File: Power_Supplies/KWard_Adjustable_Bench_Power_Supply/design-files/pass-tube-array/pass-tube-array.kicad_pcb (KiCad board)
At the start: 2 copper layers, 142.9 x 149.2 mm, 27 parts, among them J1 Screw_Terminal_01x04, J2 Screw_Terminal_01x02, U1 6550, U2 6550, U3 6550, U4 6550

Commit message: - Use bare mounting holes. - DANGER warning in all-caps.
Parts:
- REF** (x5): value MountingHole_3.2mm_M3_DIN965_Pad -> MountingHole_3.2mm_M3_DIN965; footprint MountingHole:MountingHole_3.2mm_M3_DIN965_Pad -> MountingHole:MountingHole_3.2mm_M3_DIN965
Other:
- board text added: "DANGER! HIGH VOLTAGE!"
- board text removed: "DANGER! High Voltage!"

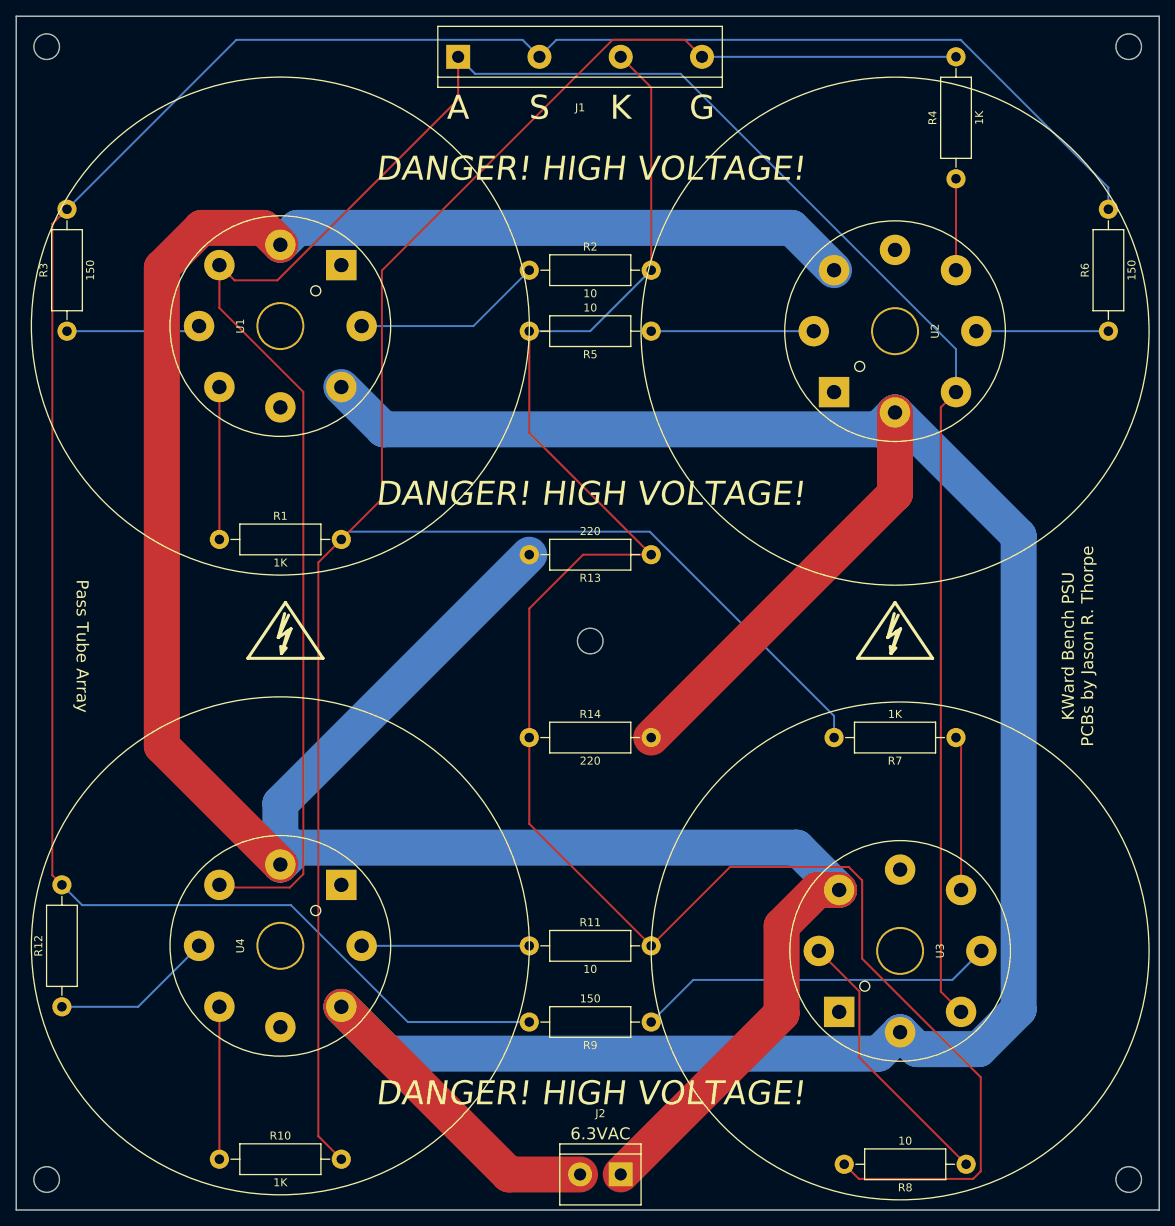
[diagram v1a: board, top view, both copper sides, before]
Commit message: Redo the pass tube array board, using the proper footprint for the AES ceramtic PC-mount octal socket.
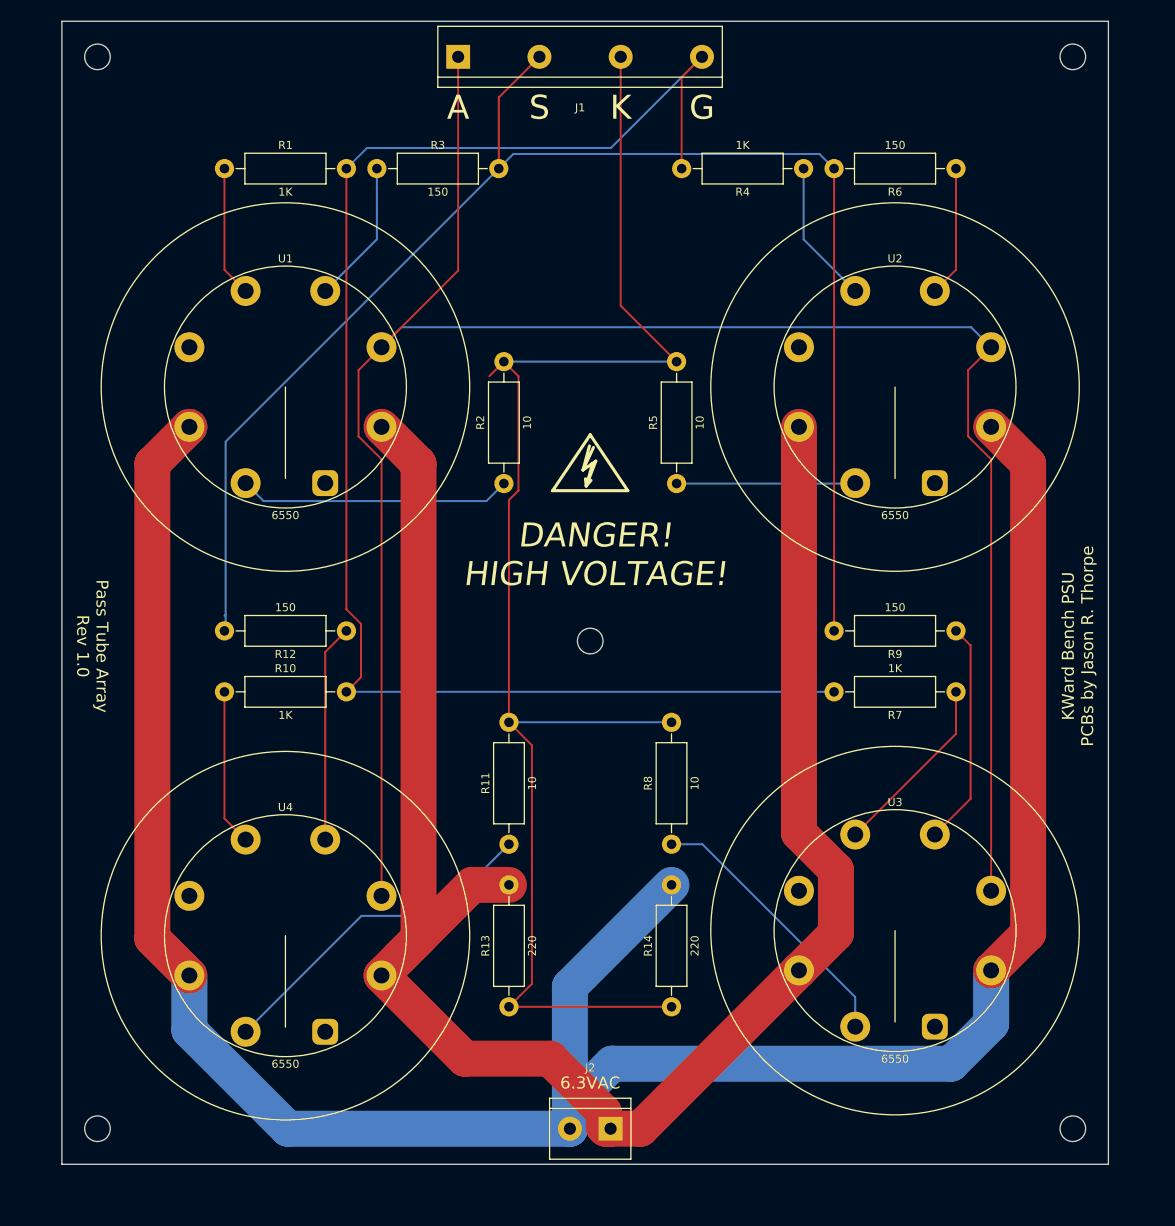
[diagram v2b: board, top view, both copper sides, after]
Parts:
- removed the REF** at (165.7, 71.1)
- removed the REF** at (165.7, 212.7)
- removed the REF** at (301.0, 212.7)
- removed the REF** at (301.0, 71.1)
- removed the REF** at (271.8, 144.8)
- added REF**: MountingHole_3.2mm_M3_DIN965, MountingHole:MountingHole_3.2mm_M3_DIN965, F.Cu at (294.0, 206.4)
- added REF**: MountingHole_3.2mm_M3_DIN965, MountingHole:MountingHole_3.2mm_M3_DIN965, F.Cu at (172.1, 206.4)
- added REF**: MountingHole_3.2mm_M3_DIN965, MountingHole:MountingHole_3.2mm_M3_DIN965, F.Cu at (172.1, 72.4)
- added REF**: MountingHole_3.2mm_M3_DIN965, MountingHole:MountingHole_3.2mm_M3_DIN965, F.Cu at (294.0, 72.4)
- U1, U2, U3, U4: footprint Valve:Valve_Octal -> jrt-TubeSockets:AES_P-ST8-193_Octal_T14
- moved R9 62.0 mm to (279.4, 144.1)
- moved R13 59.2 mm to (223.5, 191.1), turned to 90 degrees
- moved R12 58.9 mm to (203.2, 144.1), turned to 180 degrees
- moved R10 58.4 mm to (188.0, 151.8)
- moved R8 54.4 mm to (243.8, 170.8), turned to 90 degrees
- moved R1 46.4 mm to (188.0, 86.4)
- moved R3 43.7 mm to (207.0, 86.4), turned to 0 degrees
- moved REF** 43.5 mm to (233.7, 123.8)
- moved R14 38.1 mm to (243.8, 191.1), turned to 90 degrees
- moved R6 27.9 mm to (279.4, 86.4), turned to 180 degrees
- moved R2 26.9 mm to (222.9, 125.7), turned to 90 degrees
- moved R5 19.3 mm to (244.5, 125.7), turned to 90 degrees
- moved R4 19.1 mm to (260.4, 86.4), turned to 180 degrees
- moved U1 16.8 mm to (195.6, 113.7), turned to 0 degrees
- moved R11 13.0 mm to (223.5, 170.8), turned to 90 degrees
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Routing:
- net Net-(J1-Pad2): track 302.3 -> 189.5 mm
- net Filament_B: track 343.8 -> 231.1 mm
- net Net-(J1-Pad4): track 274.4 -> 193.1 mm
- net Net-(J1-Pad3): track 239.3 -> 190.1 mm
- net Net-(J1-Pad1): track 299.2 -> 259.8 mm
- net Filament_A: track 336.2 -> 306.1 mm
- net Net-(R11-Pad1): track 21.0 -> 42.6 mm
- net Net-(R9-Pad1): track 45.0 -> 28.1 mm
- net Net-(R2-Pad1): track 23.8 -> 34.1 mm
- net Net-(R12-Pad1): track 20.3 -> 27.2 mm
- net Net-(R4-Pad1): track 11.4 -> 18.0 mm
- net Net-(R7-Pad1): track 19.3 -> 23.1 mm
- net Net-(R1-Pad1): track 19.0 -> 16.4 mm
- net Net-(R5-Pad1): track 20.3 -> 22.4 mm
- net Net-(R3-Pad1): track 16.8 -> 18.0 mm
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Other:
- board size 142.9 x 149.2 mm -> 130.8 x 142.9 mm
- board text added: "Pass Tube Array Rev 1.0"
- board text removed: "Pass Tube Array"
